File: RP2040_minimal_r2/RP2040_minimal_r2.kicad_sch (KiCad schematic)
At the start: 44 parts, among them J1 SPI0.8, J10 B20, J11 B21, J12 GPIO26-29, J2 SPI0.9, J3 SPI1.13, J4 I²C0, J5 USB, J6 B16, J7 B17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

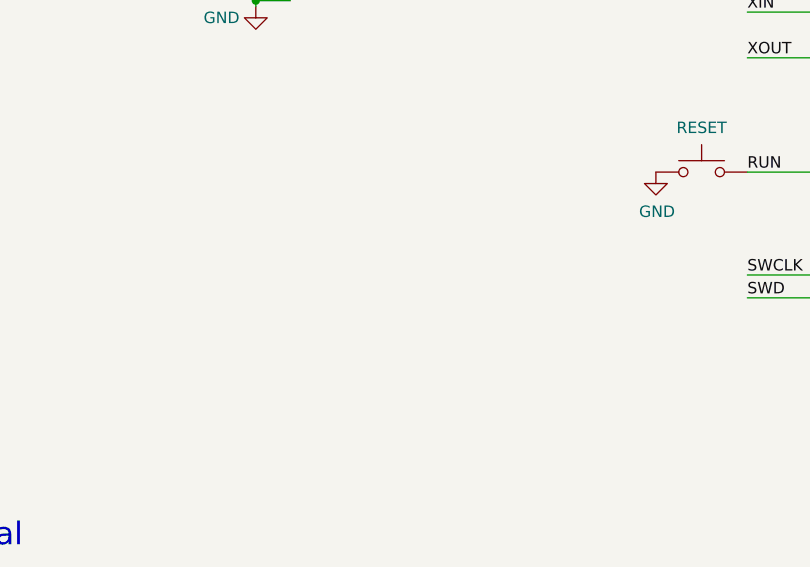
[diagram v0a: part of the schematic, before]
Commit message: Add SWD debug connector.
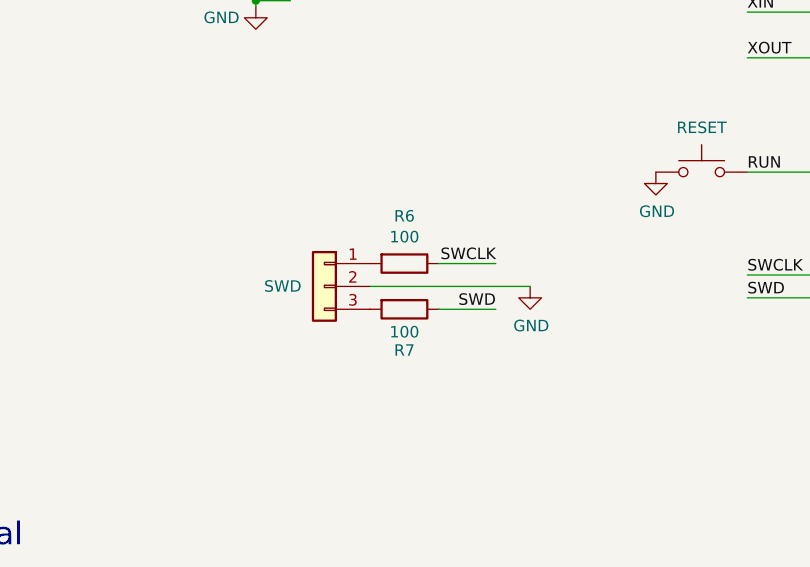
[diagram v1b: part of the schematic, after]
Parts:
- added J13: SWD, RP2040_minimal:JST_SH_BM03B-SRSS-TB_1x03-1MP_P1.00mm_Vertical, symbol Connector_Generic:Conn_01x03
- added R6, R7: 100, Resistor_SMD:R_0402_1005Metric, symbol Device:R
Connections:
- net GND: now also J13.2 (Pin_2)
- net SWCLK: now also R6.1
- net SWD: now also R7.1
- new net: J13.1 (Pin_1), R6.2
- new net: J13.3 (Pin_3), R7.2
